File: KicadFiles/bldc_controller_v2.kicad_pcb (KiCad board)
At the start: 4 copper layers, 51.5 x 89 mm, 172 parts, among them J1 Conn_01x05_Male, J10 Conn_01x02_Female, J11 Conn_01x02_Female, J12 Conn_01x02_Female, J13 Conn_01x02_Female, J14 Conn_01x02_Female, J15 Conn_01x04_Male, J2 Conn_01x03_Male, J3 Conn_01x03_Male, J4 1935174, J5 Conn_01x02_Female, J9 Conn_01x02_Female, Q10 IRLB8721PBF, Q11 IRLB8721PBF, Q2 DMN65D8L-7, Q3 DMN65D8L-7, Q5 IRF4905, Q6 IRLB8721PBF, Q7 IRLB8721PBF, Q8 IRLB8721PBF, Q9 IRLB8721PBF, SW2 D6C40 F1 LFS, SW3 1301.9314, SW4 1301.9314, SW5 SW_Push_DPDT, U1 ATmega328P-PU, U2 uA7810, U3 LM7805_TO220, U4 MCP601-xP, U5 LM339, U6 IRS2004, U7 IRS2004, U8 IRS2004, U9 HCPL-181-00DE, Y1 9B-16.000MBBK-B

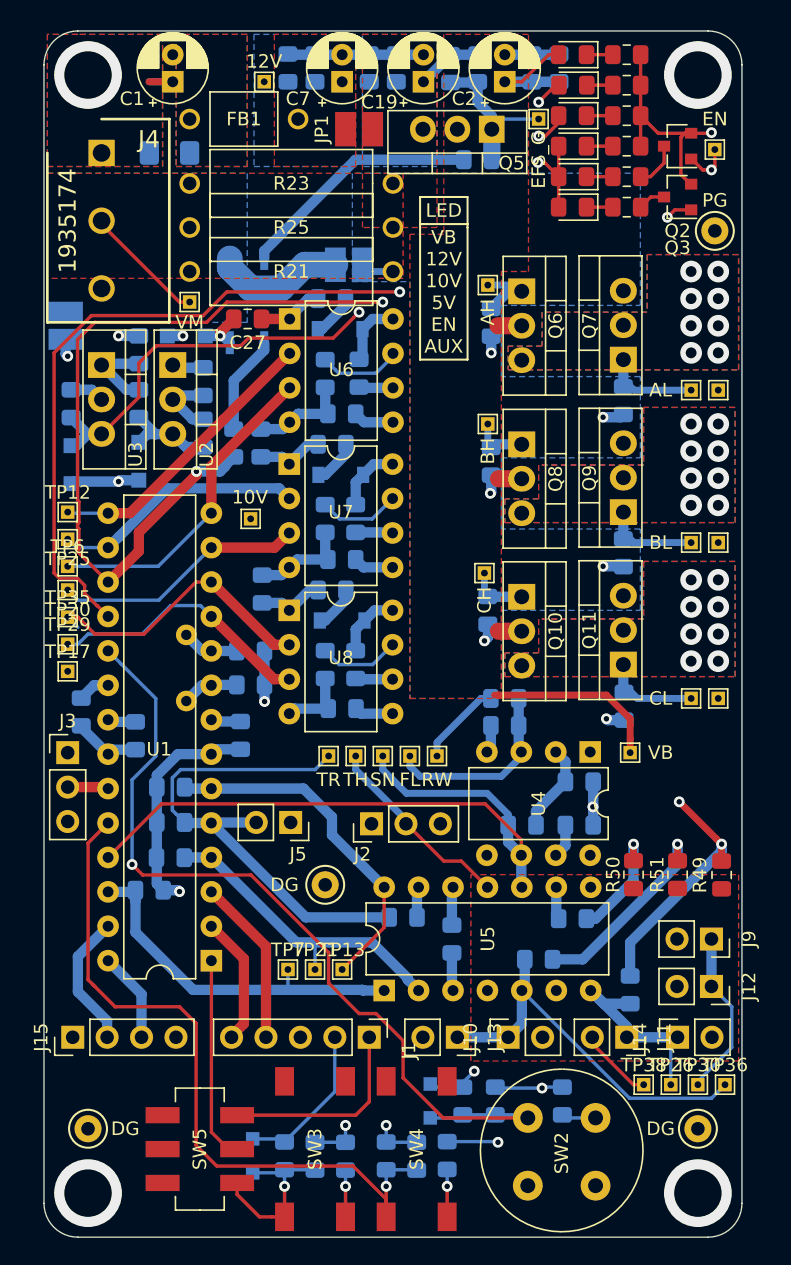
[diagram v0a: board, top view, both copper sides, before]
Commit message: Finished Top Silk
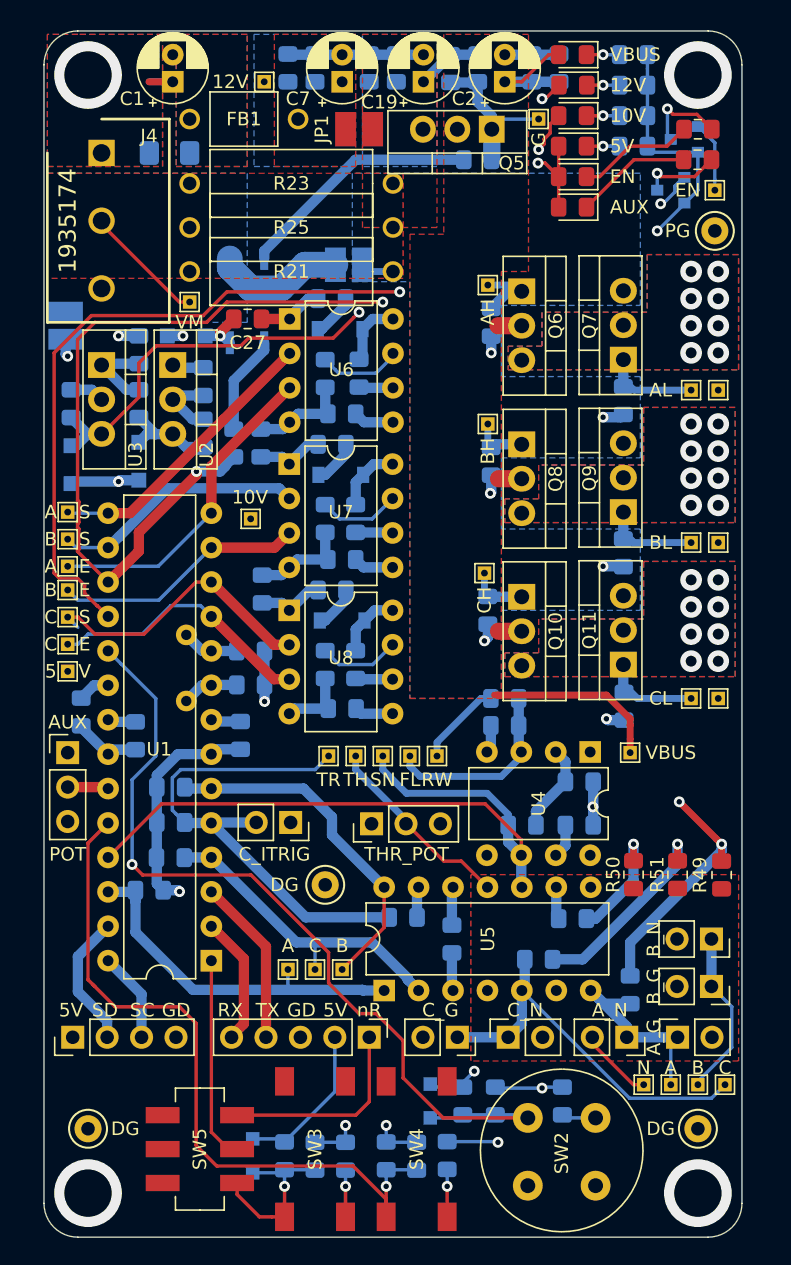
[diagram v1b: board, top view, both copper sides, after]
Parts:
- Q2, Q3, R1, R3, R5, R6: moved to B.Cu
- moved R4 6.31 mm to (161.2, 68.2)
- moved R7 6.29 mm to (161.2, 70.5)
- moved TP19 3.00 mm to (162.5, 72.8)
- moved Q2 0.71 mm to (160.2, 69.0)
- moved Q3 0.71 mm to (159.2, 72.8)
- moved R1 0.50 mm to (156.5, 62.8)
- moved R3 0.50 mm to (156.5, 65.0)
- moved R5 0.50 mm to (156.5, 67.2)
- moved R6 0.50 mm to (156.5, 69.5)
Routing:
- net GNDD: track 162.5 -> 151.6 mm
- net Net-(D6-Pad1): track 1.95 -> 8.65 mm
- net Net-(D10-Pad1): track 1.95 -> 8.62 mm
- net Net-(Q3-Pad3): track 2.04 -> 5.87 mm, vias 0 -> 1
- net Net-(Q2-Pad3): track 3.77 -> 6.28 mm, vias 0 -> 1
- net +12V: track 21.2 -> 20.4 mm
- net /AUX_OUT: track 73.3 -> 74.0 mm
- net Net-(D9-Pad1): track 1.95 -> 2.45 mm, vias 0 -> 1
- net Net-(D7-Pad1): track 1.95 -> 2.45 mm, vias 0 -> 1
- net Net-(D4-Pad1): track 1.92 -> 2.42 mm, vias 0 -> 1
- net Net-(D1-Pad1): track 1.95 -> 2.45 mm, vias 0 -> 1
- net /EFUSE_EN: track 89.6 -> 90.0 mm, vias 3 -> 2
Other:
- board text added: "5"
- board text added: "5V"
- board text added: "A"
- board text added: "AUX"
- board text added: "A_G"
- board text added: "A_N"
- board text added: "B"
- board text added: "B_G"
- board text added: "B_N"
- board text added: "C"
- board text added: "C_G"
- board text added: "C_ITRIG"
- board text added: "C_N"
- board text added: "E"
- board text added: "G"
- board text added: "GD"
- board text added: "N"
- board text added: "POT"
- board text added: "RX"
- board text added: "S"
- board text added: "SC"
- board text added: "SD"
- board text added: "THR_POT"
- board text added: "TX"
- board text added: "V"
- board text added: "VBUS"
- board text added: "nR"
- board text removed: "EFS_G"
- board text removed: "LED"
- board text removed: "VB"
- board text removed: "VB 12V 10V 5V EN AUX"

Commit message: Compated Power Section
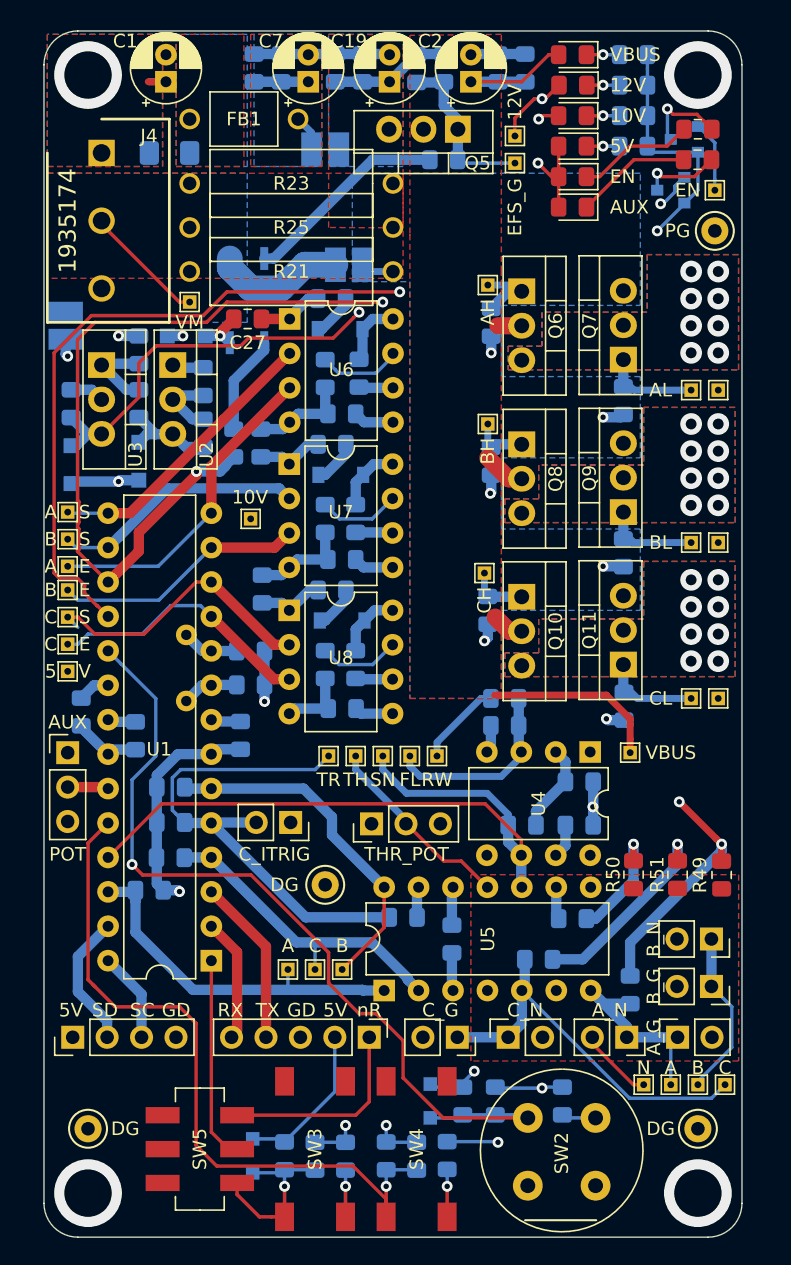
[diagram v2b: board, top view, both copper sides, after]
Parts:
- JP1: moved to B.Cu
- moved TP1 18.9 mm to (147.8, 68.8)
- moved TP11 3.69 mm to (147.8, 70.8)
- moved JP1 2.92 mm to (133.8, 69.8)
- moved C12 2.50 mm to (130.5, 63.7)
- moved C19 2.50 mm to (138.5, 64.8)
- moved C2 2.50 mm to (144.5, 64.8)
- moved C20 2.50 mm to (134.5, 63.7)
- moved C21 2.50 mm to (136.5, 63.7)
- moved C25 2.50 mm to (142.5, 63.7)
- moved C3 2.50 mm to (148.5, 63.7)
- moved C5 2.50 mm to (146.5, 63.7)
- moved C7 2.50 mm to (132.5, 64.8)
- moved C9 2.50 mm to (128.5, 63.7)
- moved Q5 2.50 mm to (143.5, 68.2)
- moved R19 2.50 mm to (140.5, 63.8)
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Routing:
- net +12V: track 20.4 -> 33.7 mm
- net VBUS: track 27.2 -> 31.8 mm
- net /V_MOTOR: track 14.0 -> 18.0 mm
- net Net-(R24-Pad2): track 18.1 -> 15.2 mm
- net +BATT: track 3.50 -> 2.56 mm
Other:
- board text added: "EFS_G"
- board text removed: "G"

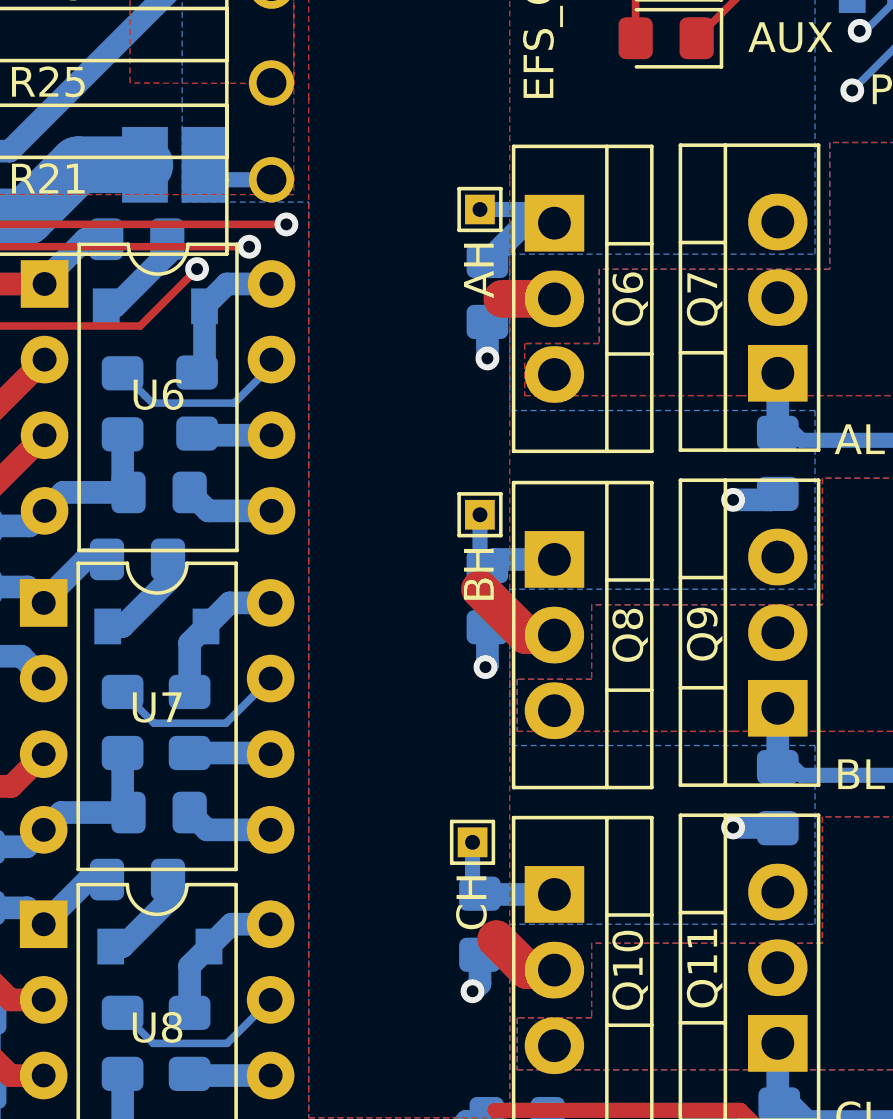
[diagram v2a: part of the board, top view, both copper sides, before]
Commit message: Fixed Gate Test Points
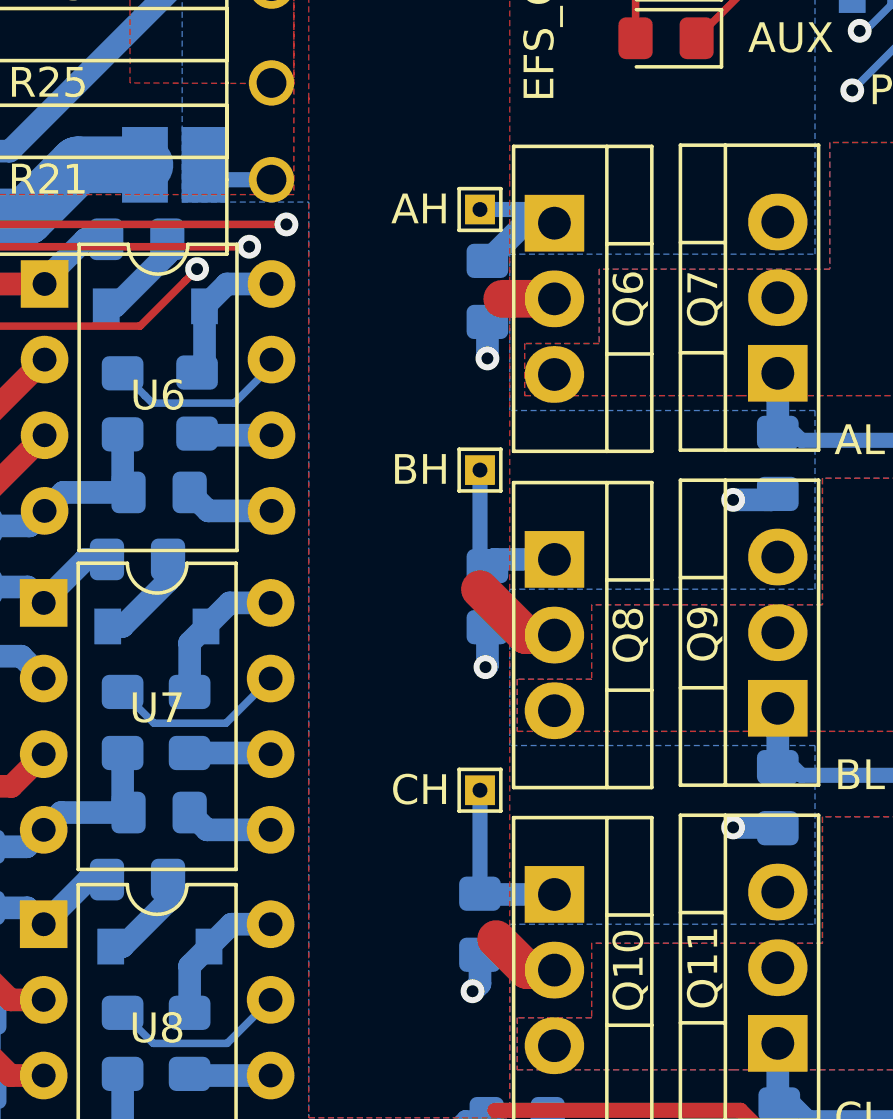
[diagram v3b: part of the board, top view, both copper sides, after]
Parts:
- moved TP32 1.77 mm to (145.8, 99.2)
- moved TP23 1.50 mm to (145.8, 88.5)
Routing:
- net /GATE_C_HI: track 4.34 -> 6.34 mm
- net /GATE_B_HI: track 4.17 -> 5.67 mm
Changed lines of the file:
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@@
   )
   (module TestPoint:TestPoint_THTPad_1.0x1.0mm_Drill0.5mm (layer F.Cu)
-    (at 145.5 101)
+    (at 145.75 99.25)
     (descr "THT rectangular pad as test Point, square 1.0mm side length, hole diameter 0.5mm")
     (tags "test point THT pad rectangle square")
@@
   )
   (module TestPoint:TestPoint_THTPad_1.0x1.0mm_Drill0.5mm (layer F.Cu)
-    (at 145.75 90)
+    (at 145.75 88.5)
     (descr "THT rectangular pad as test Point, square 1.0mm side length, hole diameter 0.5mm")
     (tags "test point THT pad rectangle square")
@@
     (effects (font (size 1 1) (thickness 0.15)))
   )
-  (gr_text CH (at 145.5 103 90) (layer F.SilkS)
+  (gr_text CH (at 143.75 99.25) (layer F.SilkS)
     (effects (font (size 1 1) (thickness 0.15)))
   )
-  (gr_text BH (at 145.75 92 90) (layer F.SilkS)
+  (gr_text BH (at 143.75 88.5) (layer F.SilkS)
     (effects (font (size 1 1) (thickness 0.15)))
   )
-  (gr_text AH (at 145.75 81.75 90) (layer F.SilkS)
+  (gr_text AH (at 143.75 79.75) (layer F.SilkS)
     (effects (font (size 1 1) (thickness 0.15)))
   )
@@
   (segment (start 148.25 91.5) (end 146.225 91.5) (width 0.762) (layer B.Cu) (net 52))
   (segment (start 145.75 91.475) (end 146 91.725) (width 0.508) (layer B.Cu) (net 52))
-  (segment (start 145.75 90) (end 145.75 91.475) (width 0.508) (layer B.Cu) (net 52))
+  (segment (start 145.75 88.5) (end 145.75 91.475) (width 0.508) (layer B.Cu) (net 52))
   (segment (start 155.75 96.5) (end 155.75 98.475) (width 0.762) (layer B.Cu) (net 53))
   (segment (start 155.75 97.9605) (end 155.75 96.5) (width 0.508) (layer B.Cu) (net 53))
@@
   (segment (start 148.25 102.75) (end 145.775 102.75) (width 0.762) (layer B.Cu) (net 54))
   (segment (start 145.5 102.475) (end 145.75 102.725) (width 0.508) (layer B.Cu) (net 54))
-  (segment (start 145.5 101) (end 145.5 102.475) (width 0.508) (layer B.Cu) (net 54))
+  (segment (start 145.75 99.25) (end 145.75 102.725) (width 0.508) (layer B.Cu) (net 54))
   (segment (start 155.75 109.75) (end 155.8 109.8) (width 0.762) (layer B.Cu) (net 55))
   (segment (start 155.75 107.75) (end 155.75 109.75) (width 0.762) (layer B.Cu) (net 55))

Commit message: Ready for DRC
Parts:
- moved J3 5.25 mm to (114.8, 119.5), turned to 180 degrees
- moved C4 4.81 mm to (115.0, 112.2), turned to 180 degrees
- moved Y1 2.00 mm to (121.5, 108.0)
- moved C8 1.46 mm to (115.0, 110.0), turned to 180 degrees
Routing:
- net +5V: track 102.6 -> 105.6 mm
- net Net-(C15-Pad2): track 4.22 -> 6.26 mm
- net Net-(C16-Pad1): track 4.22 -> 6.20 mm
- net /nESTOP: track 65.2 -> 63.8 mm
- net /MCU_C_SIG: track 21.4 -> 20.4 mm
